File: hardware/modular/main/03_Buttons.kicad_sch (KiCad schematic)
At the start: 30 parts, among them J2 COIL_L, J3 COIL_M, J4 COIL_R, U4 DRV8231ADSGR, U5 DRV8231ADSGR, U6 DRV8231ADSGR

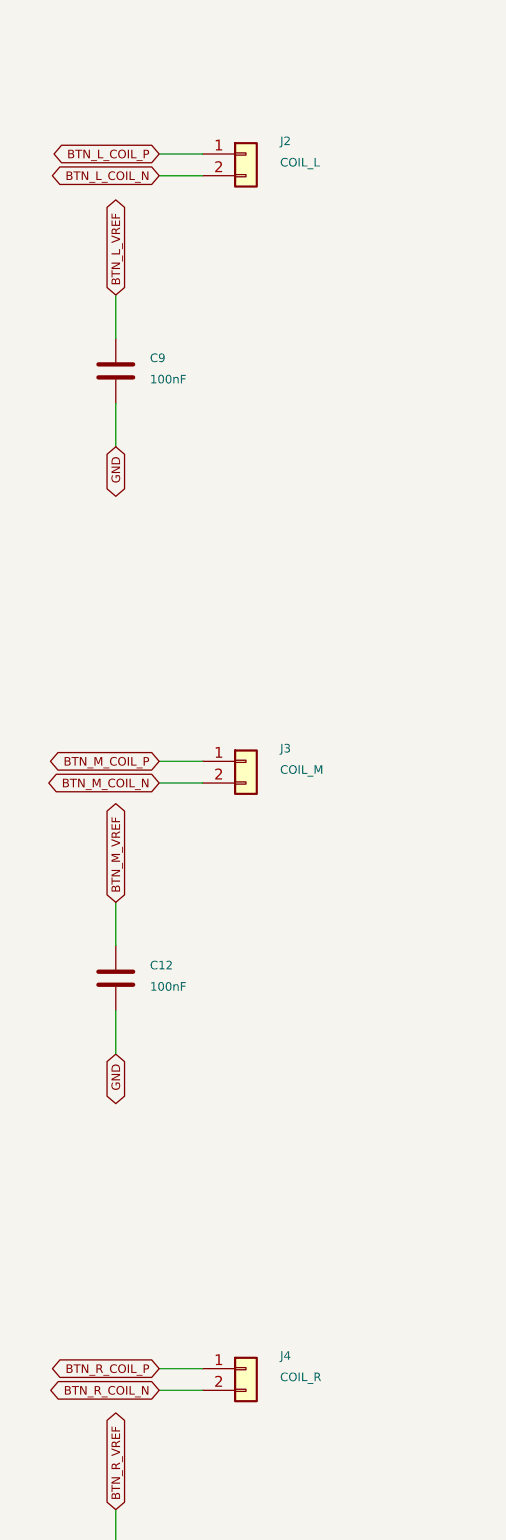
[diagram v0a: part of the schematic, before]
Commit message: Prepare wired Rev-A bench boards and submit manufacturing review
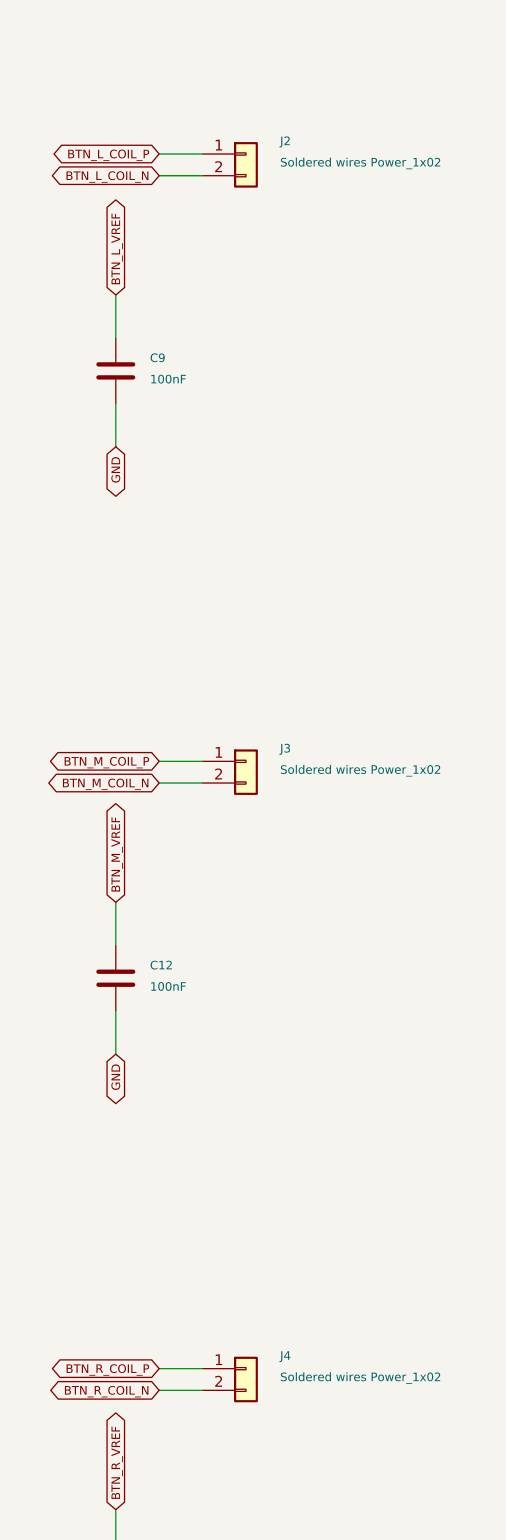
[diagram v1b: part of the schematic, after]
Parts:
- J2: value COIL_L -> Soldered wires Power_1x02; footprint Connector_JST:JST_PH_B2B-PH-SM4-TB_1x02-1MP_P2.00mm_Vertical -> MagMouseModular:Wire_Power_1x02_P2.54mm; JLCPCB Part # C265003 -> (none); LCSC C265003 -> (none); MPN B2B-PH-SM4-TBT(LF)(SN) -> (none); Manufacturer JST -> (none); Sourcing Status JLCPCB catalog verified; stock/quote refresh required -> Hand-soldered wire termination; no connector fitted; do not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; Supplier URL https://jlcpcb.com/partdetail/JST-B2B_PH_SM4_TBT_LF_SN/C265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 -> (none)
- J3: value COIL_M -> Soldered wires Power_1x02; footprint Connector_JST:JST_PH_B2B-PH-SM4-TB_1x02-1MP_P2.00mm_Vertical -> MagMouseModular:Wire_Power_1x02_P2.54mm; JLCPCB Part # C265003 -> (none); LCSC C265003 -> (none); MPN B2B-PH-SM4-TBT(LF)(SN) -> (none); Manufacturer JST -> (none); Sourcing Status JLCPCB catalog verified; stock/quote refresh required -> Hand-soldered wire termination; no connector fitted; do not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; Supplier URL https://jlcpcb.com/partdetail/JST-B2B_PH_SM4_TBT_LF_SN/C265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 -> (none)
- J4: value COIL_R -> Soldered wires Power_1x02; footprint Connector_JST:JST_PH_B2B-PH-SM4-TB_1x02-1MP_P2.00mm_Vertical -> MagMouseModular:Wire_Power_1x02_P2.54mm; JLCPCB Part # C265003 -> (none); LCSC C265003 -> (none); MPN B2B-PH-SM4-TBT(LF)(SN) -> (none); Manufacturer JST -> (none); Sourcing Status JLCPCB catalog verified; stock/quote refresh required -> Hand-soldered wire termination; no connector fitted; do not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; Supplier URL https://jlcpcb.com/partdetail/JST-B2B_PH_SM4_TBT_LF_SN/C265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 -> (none)
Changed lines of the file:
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@@
           (size 1.0 1.0))
         (justify left)))
-    (property "Value" "COIL_L"
+    (property "Value" "Soldered wires Power_1x02"
       (at 372.3 54.34 0)
       (effects
@@
           (size 1.0 1.0))
         (justify left)))
-    (property "Footprint" "Connector_JST:JST_PH_B2B-PH-SM4-TB_1x02-1MP_P2.00mm_Vertical"
+    (property "Footprint" "MagMouseModular:Wire_Power_1x02_P2.54mm"
       (at 368.3 53.34 0)
       (hide yes)
@@
           (size 1.0 1.0))
         (justify left)))
-    (property "Datasheet" "https://datasheet.lcsc.com/datasheet/pdf/91225f8a61c6f7b7821281d8757bf5b1.pdf?productCode=C2941743"
+    (property "Datasheet" ""
       (at 368.3 53.34 0)
       (hide yes)
@@
           (size 1.0 1.0))
         (justify left)))
-    (property "Manufacturer" "JST"
+    (property "Manufacturer" ""
       (at 368.3 53.34 0)
       (hide yes)
@@
           (size 1.0 1.0))
         (justify left)))
-    (property "MPN" "B2B-PH-SM4-TBT(LF)(SN)"
+    (property "MPN" ""
       (at 368.3 53.34 0)
       (hide yes)
@@
           (size 1.0 1.0))
         (justify left)))
-    (property "LCSC" "C265003"
+    (property "LCSC" ""
       (at 368.3 53.34 0)
       (hide yes)
@@
           (size 1.0 1.0))
         (justify left)))
-    (property "JLCPCB Part #" "C265003"
+    (property "JLCPCB Part #" ""
       (at 368.3 53.34 0)
       (hide yes)
@@
           (size 1.0 1.0))
         (justify left)))
-    (property "Sourcing Status" "JLCPCB catalog verified; stock/quote refresh required"
+    (property "Sourcing Status" "Hand-soldered wire termination; no connector fitted; do not fill these holes"
       (at 368.3 53.34 0)
       (hide yes)
@@
           (reference "J2")
           (unit 1))))
-    (property "Supplier URL" "https://jlcpcb.com/partdetail/JST-B2B_PH_SM4_TBT_LF_SN/C265003"
+    (property "Supplier URL" ""
       (at 368.3 53.34 0)
       (hide yes)
@@
           (size 1.0 1.0))
         (justify left)))
-    (property "Value" "COIL_M"
+    (property "Value" "Soldered wires Power_1x02"
       (at 372.3 125.46000000000001 0)
       (effects
@@
           (size 1.0 1.0))
         (justify left)))
-    (property "Footprint" "Connector_JST:JST_PH_B2B-PH-SM4-TB_1x02-1MP_P2.00mm_Vertical"
+    (property "Footprint" "MagMouseModular:Wire_Power_1x02_P2.54mm"
       (at 368.3 124.46000000000001 0)
       (hide yes)
@@
           (size 1.0 1.0))
         (justify left)))
-    (property "Datasheet" "https://datasheet.lcsc.com/datasheet/pdf/91225f8a61c6f7b7821281d8757bf5b1.pdf?productCode=C2941743"
+    (property "Datasheet" ""
       (at 368.3 124.46000000000001 0)
       (hide yes)
@@
           (size 1.0 1.0))
         (justify left)))
-    (property "Manufacturer" "JST"
+    (property "Manufacturer" ""
       (at 368.3 124.46000000000001 0)
       (hide yes)
@@
           (size 1.0 1.0))
         (justify left)))
-    (property "MPN" "B2B-PH-SM4-TBT(LF)(SN)"
+    (property "MPN" ""
       (at 368.3 124.46000000000001 0)
       (hide yes)
@@
           (size 1.0 1.0))
         (justify left)))
-    (property "LCSC" "C265003"
+    (property "LCSC" ""
       (at 368.3 124.46000000000001 0)
       (hide yes)
@@
           (size 1.0 1.0))
         (justify left)))
-    (property "JLCPCB Part #" "C265003"
+    (property "JLCPCB Part #" ""
       (at 368.3 124.46000000000001 0)
       (hide yes)
@@
           (size 1.0 1.0))
         (justify left)))
-    (property "Sourcing Status" "JLCPCB catalog verified; stock/quote refresh required"
+    (property "Sourcing Status" "Hand-soldered wire termination; no connector fitted; do not fill these holes"
       (at 368.3 124.46000000000001 0)
       (hide yes)
@@
           (reference "J3")
           (unit 1))))
-    (property "Supplier URL" "https://jlcpcb.com/partdetail/JST-B2B_PH_SM4_TBT_LF_SN/C265003"
+    (property "Supplier URL" ""
       (at 368.3 124.46000000000001 0)
       (hide yes)
@@
           (size 1.0 1.0))
         (justify left)))
-    (property "Value" "COIL_R"
+    (property "Value" "Soldered wires Power_1x02"
       (at 372.3 196.57999999999998 0)
       (effects
@@
           (size 1.0 1.0))
         (justify left)))
-    (property "Footprint" "Connector_JST:JST_PH_B2B-PH-SM4-TB_1x02-1MP_P2.00mm_Vertical"
+    (property "Footprint" "MagMouseModular:Wire_Power_1x02_P2.54mm"
       (at 368.3 195.57999999999998 0)
       (hide yes)
@@
           (size 1.0 1.0))
         (justify left)))
-    (property "Datasheet" "https://datasheet.lcsc.com/datasheet/pdf/91225f8a61c6f7b7821281d8757bf5b1.pdf?productCode=C2941743"
+    (property "Datasheet" ""
       (at 368.3 195.57999999999998 0)
       (hide yes)
@@
           (size 1.0 1.0))
         (justify left)))
-    (property "Manufacturer" "JST"
+    (property "Manufacturer" ""
       (at 368.3 195.57999999999998 0)
       (hide yes)
@@
           (size 1.0 1.0))
         (justify left)))
-    (property "MPN" "B2B-PH-SM4-TBT(LF)(SN)"
+    (property "MPN" ""
       (at 368.3 195.57999999999998 0)
       (hide yes)
@@
           (size 1.0 1.0))
         (justify left)))
-    (property "LCSC" "C265003"
+    (property "LCSC" ""
       (at 368.3 195.57999999999998 0)
       (hide yes)
@@
           (size 1.0 1.0))
         (justify left)))
-    (property "JLCPCB Part #" "C265003"
+    (property "JLCPCB Part #" ""
       (at 368.3 195.57999999999998 0)
       (hide yes)
@@
           (size 1.0 1.0))
         (justify left)))
-    (property "Sourcing Status" "JLCPCB catalog verified; stock/quote refresh required"
+    (property "Sourcing Status" "Hand-soldered wire termination; no connector fitted; do not fill these holes"
       (at 368.3 195.57999999999998 0)
       (hide yes)
@@
           (reference "J4")
           (unit 1))))
-    (property "Supplier URL" "https://jlcpcb.com/partdetail/JST-B2B_PH_SM4_TBT_LF_SN/C265003"
+    (property "Supplier URL" ""
       (at 368.3 195.57999999999998 0)
       (hide yes)
